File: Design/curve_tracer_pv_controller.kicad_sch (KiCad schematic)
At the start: 19 parts, among them J301 1720819, Q301 IPP041N12N3GXK, Q302 IRF100P218XKMA1, SW301 A20303RNCG, U301 OPA990

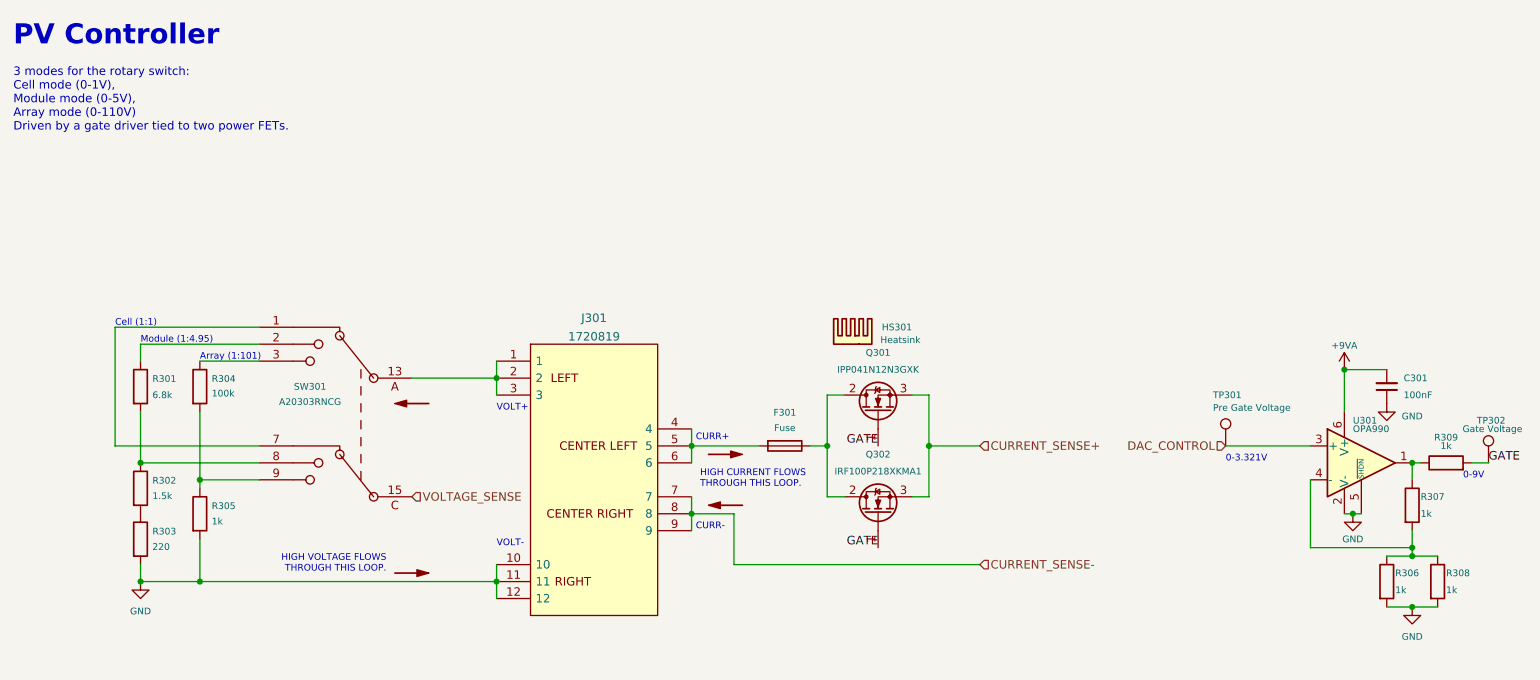
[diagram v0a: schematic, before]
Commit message: cleanup and fix errors for v1.3.0, proposed v1.4.0
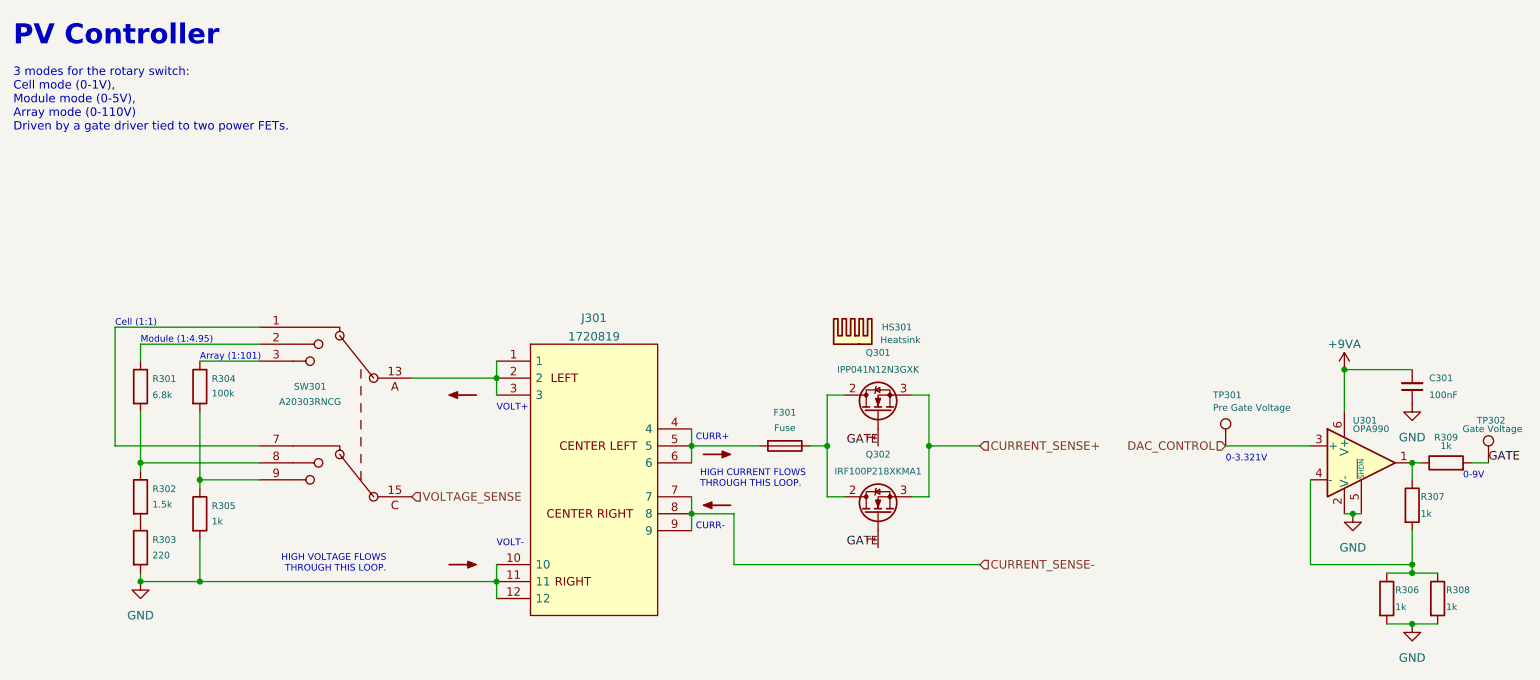
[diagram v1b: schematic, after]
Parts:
- C301: Cost (none) -> 0.0078; JLCPCB BOM 1 -> (none); LCSC Part C28233 -> (none); LCSC Part # (none) -> C28233; P/N (none) -> CL21B104KCFNNNE; Part Number N/A -> (none); Projected Cost 0.0083 -> (none); Purchase Page N/A -> (none)
- F301: Cost (none) -> 1.73; JLCPCB BOM 0 -> (none); LCSC Part N/A -> (none); P/N (none) -> 05200101Z; Part Number 576-05200101Z -> (none); Projected Cost 1.60 -> (none); Purchase Page https://www.mouser.com/ProductDetail/Littelfuse/05200101Z?q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 -> (none)
- HS301: Cost (none) -> 2.30; JLCPCB BOM 0 -> (none); LCSC Part N/A -> (none); P/N (none) -> FA-T220-38E; Part Number 588-FA-T220-38E -> (none); Projected Cost 2.09 -> (none); Purchase Page https://www.mouser.com/ProductDetail/Ohmite/FA-T220-38E?qs=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 -> (none)
- J301: Cost (none) -> 8.13; Distributor Allied -> Mouser; JLCPCB BOM 0 -> (none); LCSC Part N/A -> (none); P/N (none) -> 1720819; Part Number 1720819 -> (none); Projected Cost 7.09 -> (none); Purchase Page https://www.alliedelec.com/product/phoenix-contact/1720819/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 -> (none)
- Q301, Q302: Cost (none) -> 6.39; JLCPCB BOM 0 -> (none); LCSC Part N/A -> (none); P/N (none) -> IPP041N12N3 G; Part Number 726-IPP041N12N3GXK -> (none); Projected Cost 7.07 -> (none); Purchase Page https://www.mouser.com/ProductDetail/Infineon-Technologies/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 -> (none)
- R301: Cost (none) -> 0.0018; JLCPCB BOM 1 -> (none); LCSC Part C17772 -> (none); LCSC Part # (none) -> C17772; Manufacturer Uniroyal Elec -> UNI-ROYAL(Uniroyal Elec); P/N (none) -> 0805W8F6801T5E; Part Number N/A -> (none); Projected Cost 0.0023 -> (none); Purchase Page N/A -> (none)
- R302: Cost (none) -> 0.0018; JLCPCB BOM 1 -> (none); LCSC Part C4310 -> (none); LCSC Part # (none) -> C4310; Manufacturer Uniroyal Elec -> UNI-ROYAL(Uniroyal Elec); P/N (none) -> 0805W8F1501T5E; Part Number N/A -> (none); Projected Cost 0.0022 -> (none); Purchase Page N/A -> (none)
- R303: Cost (none) -> 0.0019; JLCPCB BOM 1 -> (none); LCSC Part C17557 -> (none); LCSC Part # (none) -> C17557; Manufacturer Uniroyal Elec -> UNI-ROYAL(Uniroyal Elec); P/N (none) -> 0805W8F2200T5E; Part Number N/A -> (none); Projected Cost 0.0023 -> (none); Purchase Page N/A -> (none)
- R304: Cost (none) -> 0.0018; JLCPCB BOM 1 -> (none); LCSC Part C149504 -> (none); LCSC Part # (none) -> C149504; Manufacturer Uniroyal Elec -> UNI-ROYAL(Uniroyal Elec); P/N (none) -> 0805W8F1003T5E; Part Number N/A -> (none); Projected Cost 0.0025 -> (none); Purchase Page N/A -> (none)
- R305, R306, R307, R308, R309: Cost (none) -> 0.0021; JLCPCB BOM 1 -> (none); LCSC Part C17513 -> (none); LCSC Part # (none) -> C17513; Manufacturer Uniroyal Elec -> UNI-ROYAL(Uniroyal Elec); P/N (none) -> 0805W8F1001T5E; Part Number N/A -> (none); Projected Cost 0.0021 -> (none); Purchase Page N/A -> (none)
- SW301: Cost (none) -> 17.70; JLCPCB BOM 0 -> (none); LCSC Part N/A -> (none); P/N (none) -> A20303RNCG; Part Number 611-A20303RNCG -> (none); Projected Cost 11.86 -> (none); Purchase Page https://www.mouser.com/ProductDetail/CK/A20303RNCG?qs=h7H1b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 -> (none)
- TP301, TP302: Part Number N/A -> (none)
- U301: Alternative Part OPA991, OPA992 -> (none); Cost (none) -> 1.31; JLCPCB BOM 0 -> (none); LCSC Part N/A -> (none); P/N (none) -> OPA990SIDBVR; Part Number OPA990SIDBVR -> (none); Projected Cost 1.30 -> (none); Purchase Page https://www.mouser.com/ProductDetail/595-OPA990SIDBVR -> (none)
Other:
- moved on the sheet: C301, R302, R303, R306, R308
